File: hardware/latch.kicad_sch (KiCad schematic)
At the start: 4 parts

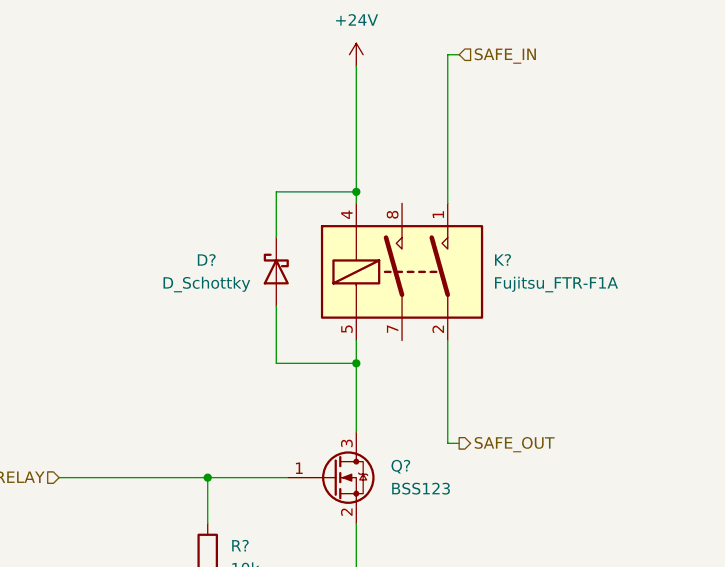
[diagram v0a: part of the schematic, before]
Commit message: Minor changes on v1 schematic
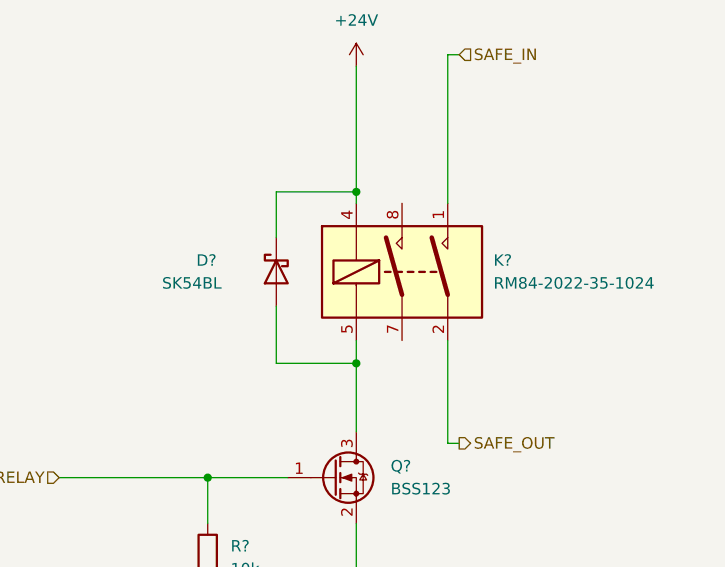
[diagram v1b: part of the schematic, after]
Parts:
- D?: value D_Schottky -> SK54BL
- K?: value Fujitsu_FTR-F1A -> RM84-2022-35-1024
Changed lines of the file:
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@@
       (effects (font (size 1.27 1.27)) (justify right))
     )
-    (property "Value" "D_Schottky" (id 1) (at 116.84 110.49 90)
+    (property "Value" "SK54BL" (id 1) (at 116.84 110.49 90)
       (effects (font (size 1.27 1.27)) (justify right))
     )
@@
       (effects (font (size 1.27 1.27)) (justify right))
     )
-    (property "Value" "Fujitsu_FTR-F1A" (id 1) (at 153.67 110.4899 90)
+    (property "Value" "RM84-2022-35-1024" (id 1) (at 153.67 110.4899 90)
       (effects (font (size 1.27 1.27)) (justify right))
     )

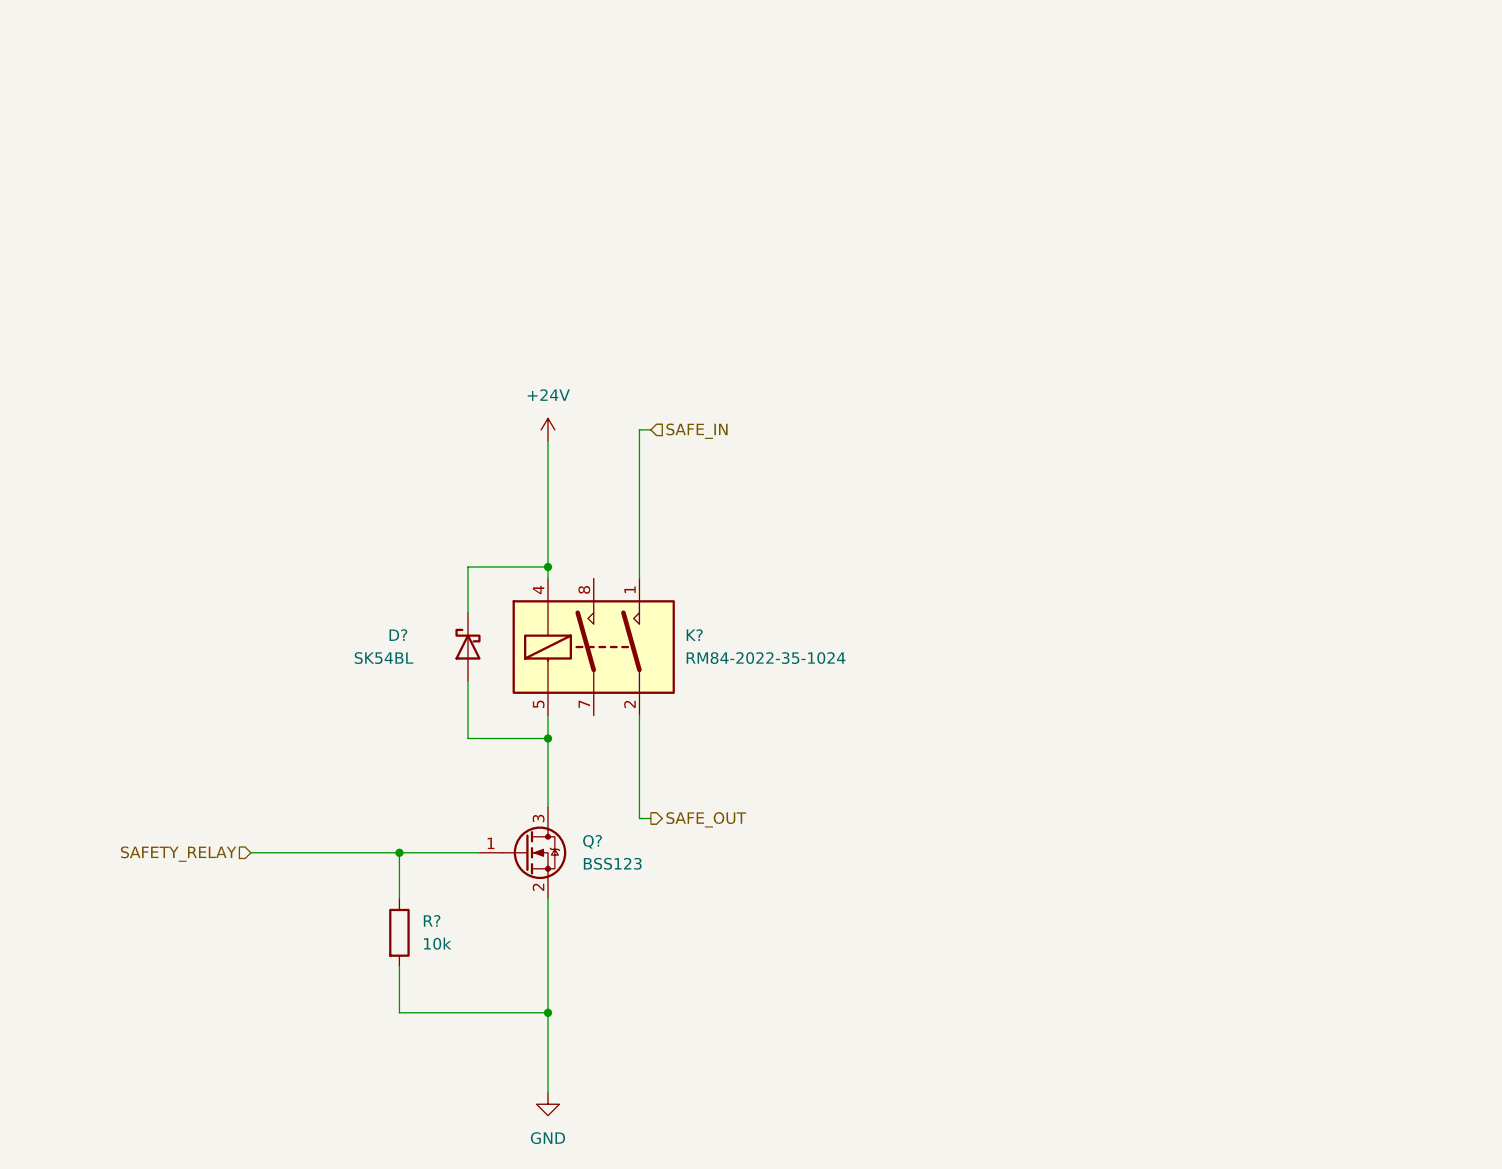
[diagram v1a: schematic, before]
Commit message: minor schematic cleanup
Fixes before second review
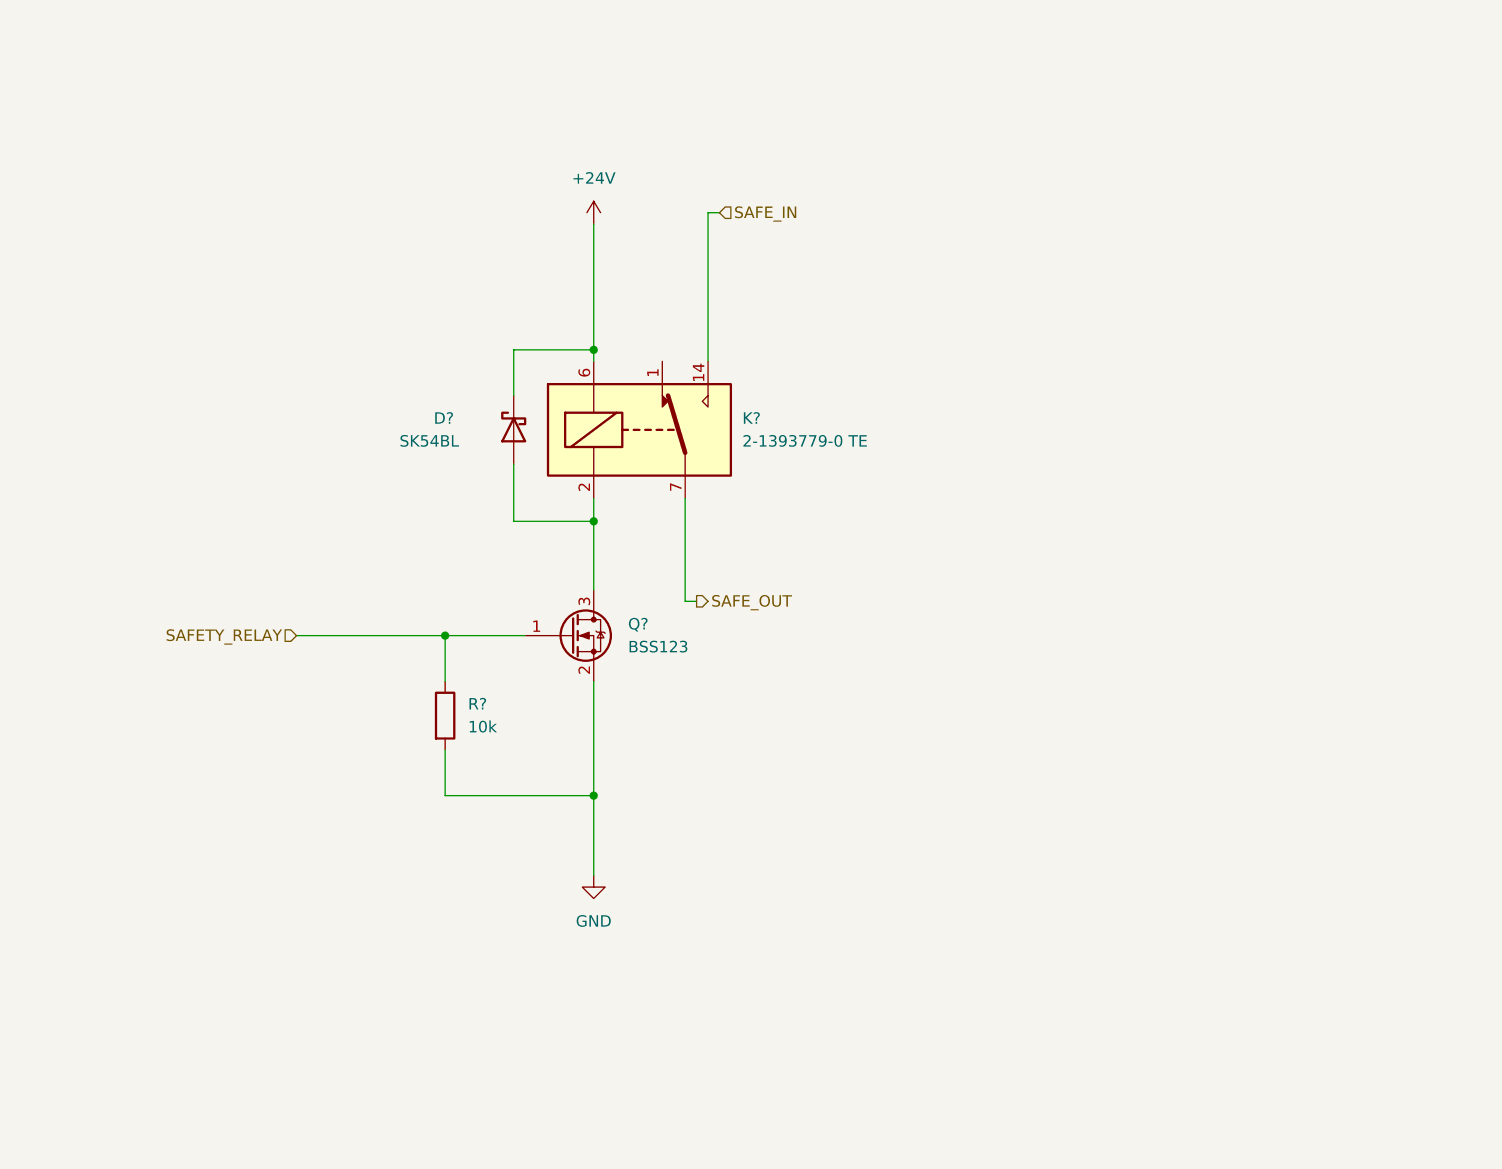
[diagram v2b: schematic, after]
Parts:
- removed K?: RM84-2022-35-1024, Relay_THT:Relay_DPST_Fujitsu_FTR-F1A, symbol Relay:Fujitsu_FTR-F1A
- added K?: 2-1393779-0 TE, Relay_THT:Relay_StandexMeder_DIP_LowProfile, symbol Relay:DIPxx-1Cxx-51x
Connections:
- net +24V: now also K?.6
- net SAFE_IN: now also K?.14
- net SAFE_OUT: now also K?.7, K?.8
- net at D?.2 (A), Q?.3 (D): now also K?.2
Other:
- company: (none) -> PUT Motorsport
- title: (none) -> SDC Relay
- moved on the sheet: D?, Q?, R?

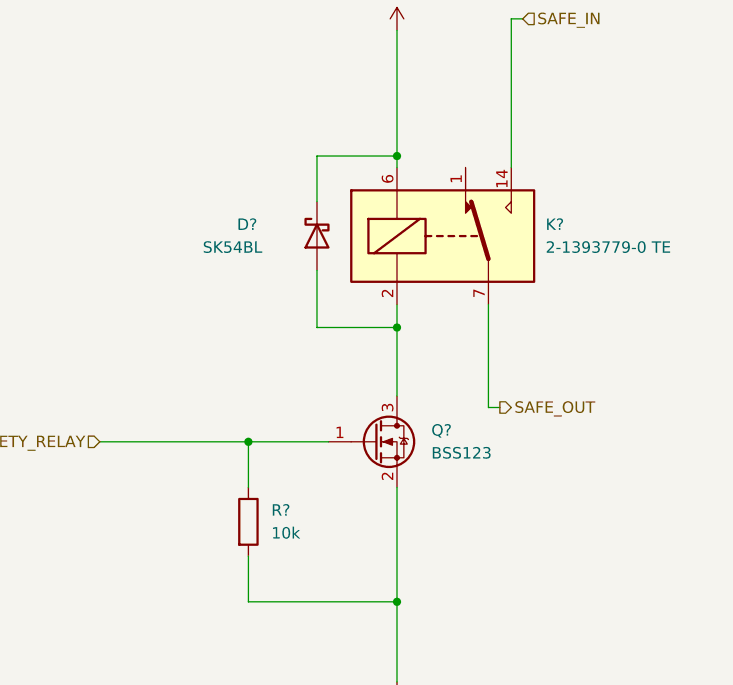
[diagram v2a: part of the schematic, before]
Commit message: Schematic ready for second review
Cleaned up, numerated, added footprints, JW notes considered
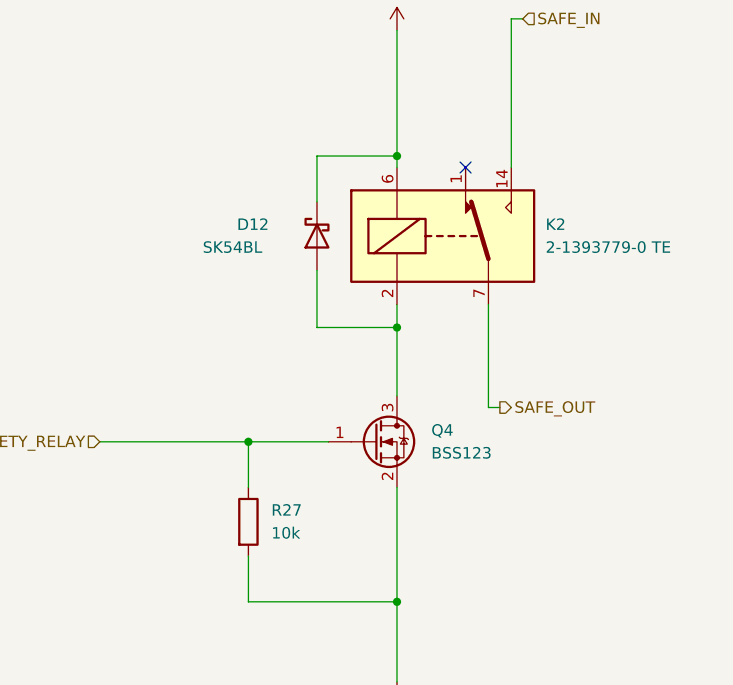
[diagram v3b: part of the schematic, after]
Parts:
- D12: renamed from D?; footprint (none) -> Diode_SMD:D_SMB
- R27: renamed from R?; footprint (none) -> Resistor_SMD:R_0603_1608Metric
- gave numbers to parts that had none: 2
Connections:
- no-connect marks 0 -> 1
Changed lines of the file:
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@@
   (junction (at 143.51 95.25) (diameter 0) (color 0 0 0 0)
   )
+  (no_connect (at 151.13 77.47))
   (wire (pts (xy 110.49 107.95) (xy 127 107.95))
     (stroke (width 0) (type default) (color 0 0 0 0))
@@
   (symbol (lib_id "Relay:DIPxx-1Cxx-51x") (at 148.59 85.09 0) (unit 1)
     (in_bom yes) (on_board yes) (fields_autoplaced)
-    (property "Reference" "K?" (id 0) (at 160.02 83.8199 0)
+    (property "Reference" "K2" (id 0) (at 160.02 83.8199 0)
       (effects (font (size 1.27 1.27)) (justify left))
     )
@@
   (symbol (lib_id "power:GND") (at 143.51 134.62 0) (unit 1)
     (in_bom yes) (on_board yes) (fields_autoplaced)
-    (property "Reference" "#PWR?" (id 0) (at 143.51 140.97 0)
+    (property "Reference" "#PWR044" (id 0) (at 143.51 140.97 0)
       (effects (font (size 1.27 1.27)) hide)
     )
@@
   (symbol (lib_id "Transistor_FET:BSS123") (at 140.97 107.95 0) (unit 1)
     (in_bom yes) (on_board yes) (fields_autoplaced)
-    (property "Reference" "Q?" (id 0) (at 147.32 106.6799 0)
+    (property "Reference" "Q4" (id 0) (at 147.32 106.6799 0)
       (effects (font (size 1.27 1.27)) (justify left))
     )
@@
   (symbol (lib_id "Device:D_Schottky") (at 134.62 85.09 90) (mirror x) (unit 1)
     (in_bom yes) (on_board yes)
-    (property "Reference" "D?" (id 0) (at 125.73 83.82 90)
+    (property "Reference" "D12" (id 0) (at 125.73 83.82 90)
       (effects (font (size 1.27 1.27)) (justify right))
     )
@@
       (effects (font (size 1.27 1.27)) (justify right))
     )
-    (property "Footprint" "" (id 2) (at 134.62 85.09 0)
+    (property "Footprint" "Diode_SMD:D_SMB" (id 2) (at 134.62 85.09 0)
       (effects (font (size 1.27 1.27)) hide)
     )
@@
   (symbol (lib_id "power:+24V") (at 143.51 62.23 0) (unit 1)
     (in_bom yes) (on_board yes) (fields_autoplaced)
-    (property "Reference" "#PWR?" (id 0) (at 143.51 66.04 0)
+    (property "Reference" "#PWR043" (id 0) (at 143.51 66.04 0)
       (effects (font (size 1.27 1.27)) hide)
     )
@@
   (symbol (lib_id "Device:R") (at 127 116.84 0) (unit 1)
     (in_bom yes) (on_board yes) (fields_autoplaced)
-    (property "Reference" "R?" (id 0) (at 129.54 115.5699 0)
+    (property "Reference" "R27" (id 0) (at 129.54 115.5699 0)
       (effects (font (size 1.27 1.27)) (justify left))
     )
@@
       (effects (font (size 1.27 1.27)) (justify left))
     )
-    (property "Footprint" "" (id 2) (at 125.222 116.84 90)
+    (property "Footprint" "Resistor_SMD:R_0603_1608Metric" (id 2) (at 125.222 116.84 90)
       (effects (font (size 1.27 1.27)) hide)
     )
